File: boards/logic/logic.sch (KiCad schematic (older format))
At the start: 39 parts

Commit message: Add a pullup resistor to CH_PD.
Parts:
- added R?: 10k, symbol R
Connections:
- net +3V3: now also R?.2; no longer U?.3 (CH_PD)
- new net: R?.1, U?.3 (CH_PD)
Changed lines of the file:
@@
 LIBS:cb2-cache
 LIBS:lcdb4-cache
-LIBS:A20Clock_Logic-cache
+LIBS:logic-cache
 EELAYER 25 0
 EELAYER END
@@
 	625  6025 625  6225
 Wire Wire Line
-	625  6225 1450 6225
-Wire Wire Line
 	6275 6575 6375 6575
 Wire Wire Line
@@
 Wire Wire Line
 	2225 4650 2225 4450
+$Comp
+L R R?
+U 1 1 57D47C26
+P 1025 6225
+F 0 "R?" V 1105 6225 50  0000 C CNN
+F 1 "10k" V 1025 6225 50  0000 C CNN
+F 2 "" V 955 6225 50  0000 C CNN
+F 3 "" H 1025 6225 50  0000 C CNN
+	1    1025 6225
+	0    1    1    0
+$EndComp
+Wire Wire Line
+	625  6225 875  6225
+Wire Wire Line
+	1175 6225 1450 6225
 $EndSCHEMATC

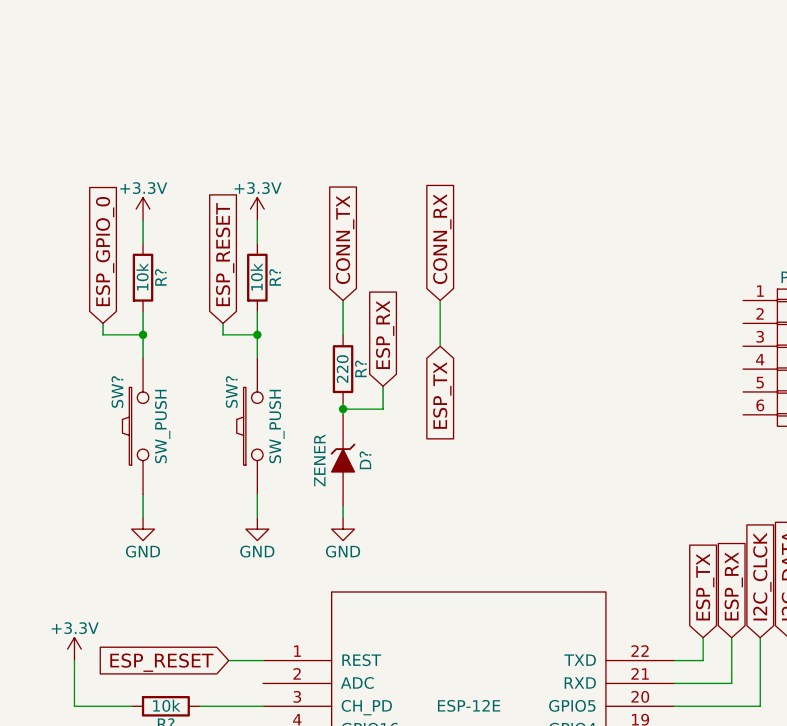
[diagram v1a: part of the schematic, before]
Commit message: Remove the level shifter (via zener) from the CONN_TX->ESP_RX connection.
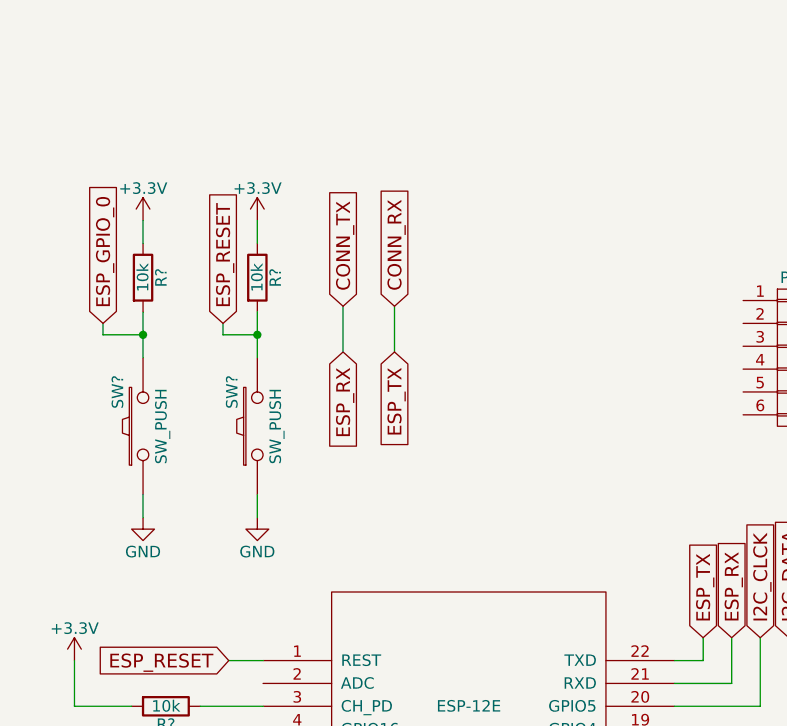
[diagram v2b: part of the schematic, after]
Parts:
- removed D?: ZENER, symbol ZENER
- removed R?: 220, symbol R
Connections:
- net ESP_RX is gone; now on net CONN_TX: U?.21 (RXD)
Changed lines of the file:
@@
 	1    0    0    -1
 $EndComp
-$Comp
-L ZENER D?
-U 1 1 57754907
-P 1800 5150
-F 0 "D?" H 1800 5250 50  0000 C CNN
-F 1 "ZENER" H 1800 5050 50  0000 C CNN
-F 2 "" H 1800 5150 50  0000 C CNN
-F 3 "" H 1800 5150 50  0000 C CNN
-	1    1800 5150
-	0    1    1    0
-$EndComp
-Text GLabel 1800 4450 1    60   Input ~ 0
+Text GLabel 1800 4475 1    60   Input ~ 0
 CONN_TX
-Text GLabel 2225 4450 1    60   Input ~ 0
+Text GLabel 2025 4475 1    60   Input ~ 0
 CONN_RX
-$Comp
-L R R?
-U 1 1 57754CBA
-P 1800 4750
-F 0 "R?" V 1880 4750 50  0000 C CNN
-F 1 "220" V 1800 4750 50  0000 C CNN
-F 2 "" V 1730 4750 50  0000 C CNN
-F 3 "" H 1800 4750 50  0000 C CNN
-	1    1800 4750
-	1    0    0    -1
-$EndComp
-$Comp
-L GND #PWR?
-U 1 1 57755002
-P 1800 5400
-F 0 "#PWR?" H 1800 5150 50  0001 C CNN
-F 1 "GND" H 1800 5250 50  0000 C CNN
-F 2 "" H 1800 5400 50  0000 C CNN
-F 3 "" H 1800 5400 50  0000 C CNN
-	1    1800 5400
-	1    0    0    -1
-$EndComp
-Text GLabel 1975 4825 1    60   Input ~ 0
+Text GLabel 1800 4675 3    60   Input ~ 0
 ESP_RX
 Wire Wire Line
@@
 	1550 875  1650 875
 Connection ~ 1600 875
-Wire Wire Line
-	1800 4450 1800 4600
-Wire Wire Line
-	1800 4925 1975 4925
-Wire Wire Line
-	1800 4900 1800 4950
-Connection ~ 1800 4925
-Wire Wire Line
-	1800 5350 1800 5400
-Wire Wire Line
-	1975 4925 1975 4825
-Text GLabel 2225 4650 3    60   Input ~ 0
+Text GLabel 2025 4675 3    60   Input ~ 0
 ESP_TX
 Wire Wire Line
-	2225 4650 2225 4450
+	2025 4675 2025 4475
 $Comp
 L R R?
@@
 Wire Wire Line
 	1175 6225 1450 6225
+Wire Wire Line
+	1800 4475 1800 4675
 $EndSCHEMATC
